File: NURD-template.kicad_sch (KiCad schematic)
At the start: 4 parts

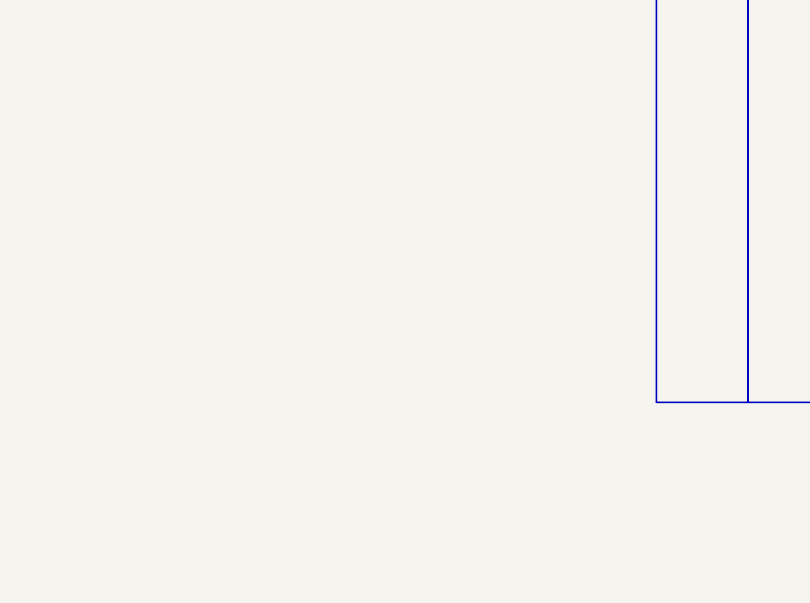
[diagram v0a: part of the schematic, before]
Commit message: Added MP2731
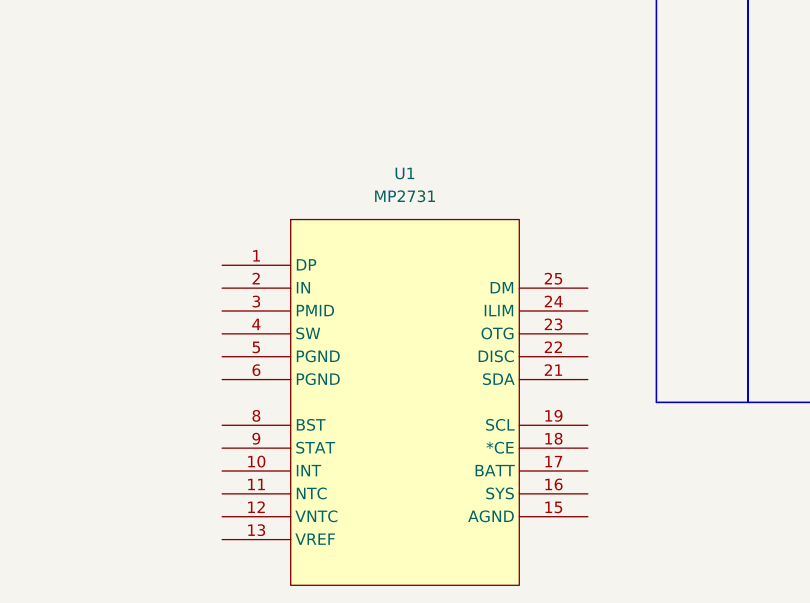
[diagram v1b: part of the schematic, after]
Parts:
- added U1: MP2731, 0_NRD_footprints:MPS_QFN-26-35mmx35mm, symbol 0_NRD_Switchers:BCK_MPS_MP2731
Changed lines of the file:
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@@
+	)
+	(symbol
+		(lib_id "0_NRD_Switchers:BCK_MPS_MP2731")
+		(at 156.21 102.87 0)
+		(unit 1)
+		(exclude_from_sim no)
+		(in_bom yes)
+		(on_board yes)
+		(dnp no)
+		(fields_autoplaced yes)
+		(property "Reference" "U1"
+			(at 156.21 77.47 0)
+			(effects
+				(font
+					(size 1.27 1.27)
+				)
+			)
+		)
+		(property "Value" "MP2731"
+			(at 156.21 80.01 0)
+			(effects
+				(font
+					(size 1.27 1.27)
+				)
+			)
+		)
+		(property "Footprint" "0_NRD_footprints:MPS_QFN-26-35mmx35mm"
+			(at 156.718 64.262 0)
+			(effects
+				(font
+					(size 1.27 1.27)
+				)
+				(hide yes)
+			)
+		)
+		(property "Datasheet" "https://www.monolithicpower.com/en/documentview/productdocument/index/version/2/document_type/Datasheet/lang/en/sku/MP2731GQC/?srsltid=AfmBOoqsVkOYvXxeOVLr7tGCJUOepRgahuh0kIY-v4QbYAHyos3XwziO"
+			(at 156.464 64.262 0)
+			(effects
+				(font
+					(size 1.27 1.27)
+				)
+				(hide yes)
+			)
+		)
+		(property "Description" "Battery Charger, Single Cell of Li-Ion Battery, 5.5 V input, 4.67 V / 4.5 A Charge, QFN-16"
+			(at 155.702 64.262 0)
+			(effects
+				(font
+					(size 1.27 1.27)
+				)
+				(hide yes)
+			)
+		)
+		(property "S1 Price @ 100" "1.43"
+			(at 155.702 64.262 0)
+			(effects
+				(font
+					(size 1.27 1.27)
+				)
+				(hide yes)
+			)
+		)
+		(property "S1 Part number" "3795967"
+			(at 155.702 64.262 0)
+			(effects
+				(font
+					(size 1.27 1.27)
+				)
+				(hide yes)
+			)
+		)
+		(property "MPN" "MP2731GQC-0000-P"
+			(at 155.702 64.262 0)
+			(effects
+				(font
+					(size 1.27 1.27)
+				)
+				(hide yes)
+			)
+		)
+		(property "MF" "MPS"
+			(at 155.702 64.262 0)
+			(effects
+				(font
+					(size 1.27 1.27)
+				)
+				(hide yes)
+			)
+		)
+		(property "S1 Part link" "https://nl.farnell.com/monolithic-power-systems-mps/mp2731gqc-0000-p/battery-charger-li-ion-pol-125deg/dp/3795967"
+			(at 155.702 64.262 0)
+			(effects
+				(font
+					(size 1.27 1.27)
+				)
+				(hide yes)
+			)
+		)
+		(property "S1 Description" "Battery Charger, Single Cell of Li-Ion Battery, 5.5 V input, 4.67 V / 4.5 A Charge, QFN-16"
+			(at 155.702 64.262 0)
+			(effects
+				(font
+					(size 1.27 1.27)
+				)
+				(hide yes)
+			)
+		)
+		(property "Update date" "13-04-2026"
+			(at 155.702 64.262 0)
+			(effects
+				(font
+					(size 1.27 1.27)
+				)
+				(hide yes)
+			)
+		)
+		(property "Notes" ""
+			(at 155.448 64.516 0)
+			(effects
+				(font
+					(size 1.27 1.27)
+				)
+				(hide yes)
+			)
+		)
+		(pin "13"
+		)
+		(pin "23"
+		)
+		(pin "21"
+		)
+		(pin "22"
+		)
+		(pin "10"
+		)
+		(pin "25"
+		)
+		(pin "8"
+		)
+		(pin "4"
+		)
+		(pin "5"
+		)
+		(pin "6"
+		)
+		(pin "9"
+		)
+		(pin "1"
+		)
+		(pin "2"
+		)
+		(pin "3"
+		)
+		(pin "11"
+		)
+		(pin "12"
+		)
+		(pin "24"
+		)
+		(pin "15"
+		)
+		(pin "18"
+		)
+		(pin "19"
+		)
+		(pin "17"
+		)
+		(pin "16"
+		)
+		(instances
+			(project ""
+				(path "/1b1d42dc-f63c-49d9-9b61-b09c30b6ea01"
+					(reference "U1")
+					(unit 1)
+				)
+			)
+		)
 	)
 	(symbol

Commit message: Updated to KiCAD 10
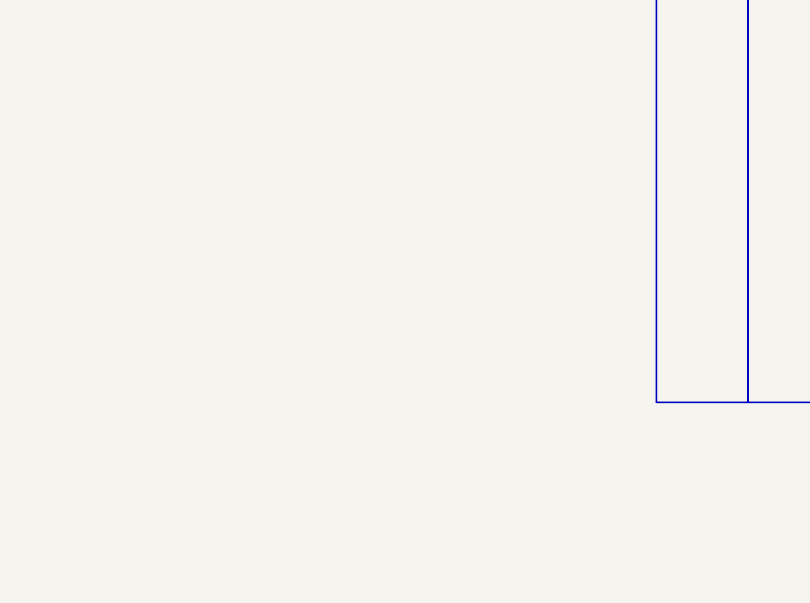
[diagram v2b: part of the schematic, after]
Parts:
- removed U1: MP2731, 0_NRD_footprints:MPS_QFN-26-35mmx35mm, symbol 0_NRD_Switchers:BCK_MPS_MP2731
